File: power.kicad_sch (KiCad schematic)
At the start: 34 parts, among them J1 +5V SUPPLY, SW1 RESET, U1 NS32201, U2 LM3671, U3 NS32016, U4 NS32082, U5 NS32202, U6 74AHC08, Y1 12.00000MHz

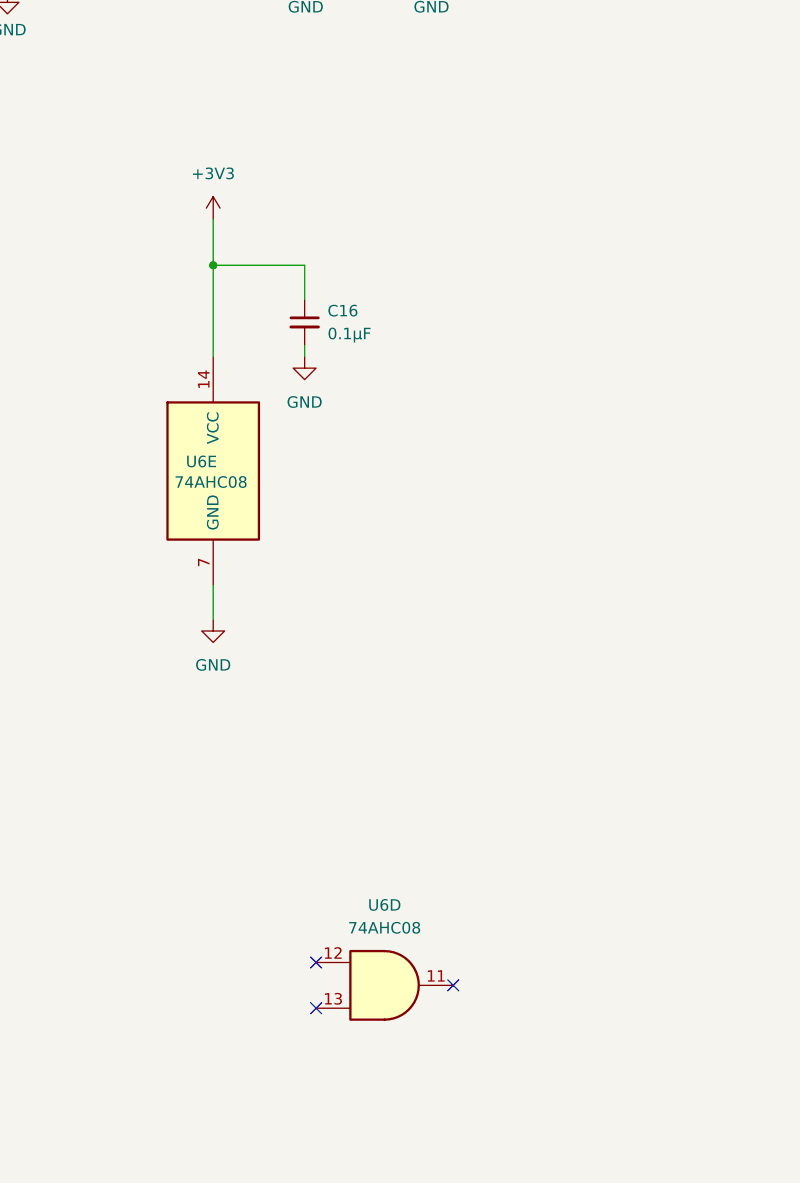
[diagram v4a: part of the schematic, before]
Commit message: add buffer to ICU
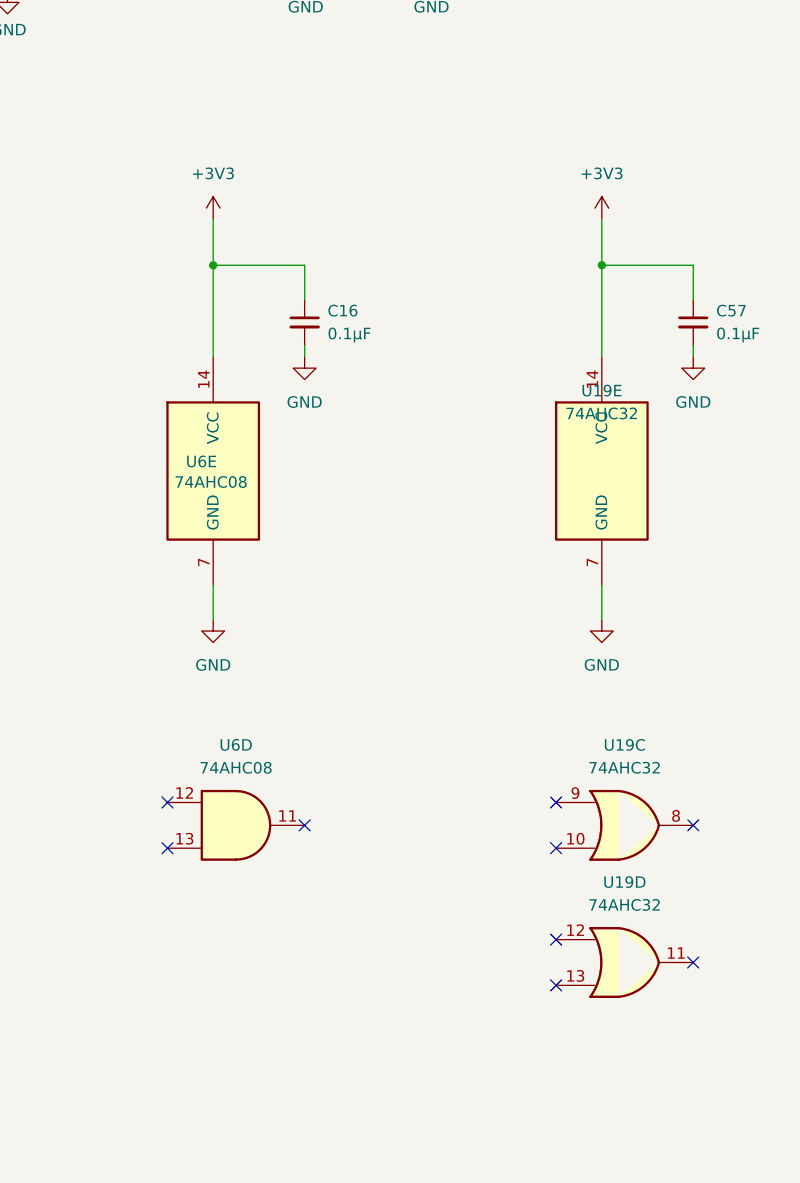
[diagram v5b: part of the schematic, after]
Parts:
- added C57: 0.1µF, Capacitor_SMD:C_0402_1005Metric, symbol Device:C_Small
- added U19: 74AHC32, Package_SO:TSSOP-14_4.4x5mm_P0.65mm, symbol 74xx:74LS32
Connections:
- net +3V3: now also C57.1, U19.14 (VCC)
- net GND: now also C57.2, U19.7 (GND)
- no-connect marks 4 -> 10
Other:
- moved on the sheet: U6D

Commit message: add 33uF 1206 16V reservoir cap to 5V
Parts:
- added C59: 33µF 16V, Capacitor_SMD:C_1206_3216Metric, symbol Device:C_Small
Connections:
- net +5V: now also C59.1
- net GND: now also C59.2
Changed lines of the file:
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@@
 	(wire
 		(pts
+			(xy 270.51 49.53) (xy 270.51 52.07)
+		)
+		(stroke
+			(width 0)
+			(type default)
+		)
+	)
+	(wire
+		(pts
 			(xy 147.32 43.18) (xy 147.32 40.64)
 		)
@@
 	(wire
 		(pts
+			(xy 270.51 41.91) (xy 270.51 44.45)
+		)
+		(stroke
+			(width 0)
+			(type default)
+		)
+	)
+	(wire
+		(pts
 			(xy 133.35 87.63) (xy 133.35 91.44)
 		)
@@
 	(symbol
 		(lib_id "power:GND")
+		(at 270.51 52.07 0)
+		(unit 1)
+		(exclude_from_sim no)
+		(in_bom yes)
+		(on_board yes)
+		(dnp no)
+		(fields_autoplaced yes)
+		(property "Reference" "#PWR0150"
+			(at 270.51 58.42 0)
+			(effects
+				(font
+					(size 1.27 1.27)
+				)
+				(hide yes)
+			)
+		)
+		(property "Value" "GND"
+			(at 270.51 57.15 0)
+			(effects
+				(font
+					(size 1.27 1.27)
+				)
+			)
+		)
+		(property "Footprint" ""
+			(at 270.51 52.07 0)
+			(effects
+				(font
+					(size 1.27 1.27)
+				)
+				(hide yes)
+			)
+		)
+		(property "Datasheet" ""
+			(at 270.51 52.07 0)
+			(effects
+				(font
+					(size 1.27 1.27)
+				)
+				(hide yes)
+			)
+		)
+		(property "Description" "Power symbol creates a global label with name \"GND\" , ground"
+			(at 270.51 52.07 0)
+			(effects
+				(font
+					(size 1.27 1.27)
+				)
+				(hide yes)
+			)
+		)
+		(pin "1"
+		)
+		(instances
+			(project ""
+				(path "/54787df0-1b8c-465f-acae-f55ec7f02da3/c6a0d4a9-2340-4a27-802f-10b03153dcd5"
+					(reference "#PWR0150")
+					(unit 1)
+				)
+			)
+		)
+	)
+	(symbol
+		(lib_id "power:GND")
 		(at 76.2 105.41 0)
 		(unit 1)
@@
 	)
 	(symbol
+		(lib_id "Device:C_Small")
+		(at 270.51 46.99 0)
+		(unit 1)
+		(exclude_from_sim no)
+		(in_bom yes)
+		(on_board yes)
+		(dnp no)
+		(fields_autoplaced yes)
+		(property "Reference" "C59"
+			(at 273.05 45.7262 0)
+			(effects
+				(font
+					(size 1.27 1.27)
+				)
+				(justify left)
+			)
+		)
+		(property "Value" "33µF 16V"
+			(at 273.05 48.2662 0)
+			(effects
+				(font
+					(size 1.27 1.27)
+				)
+				(justify left)
+			)
+		)
+		(property "Footprint" "Capacitor_SMD:C_1206_3216Metric"
+			(at 270.51 46.99 0)
+			(effects
+				(font
+					(size 1.27 1.27)
+				)
+				(hide yes)
+			)
+		)
+		(property "Datasheet" "~"
+			(at 270.51 46.99 0)
+			(effects
+				(font
+					(size 1.27 1.27)
+				)
+				(hide yes)
+			)
+		)
+		(property "Description" "Unpolarized capacitor, small symbol"
+			(at 270.51 46.99 0)
+			(effects
+				(font
+					(size 1.27 1.27)
+				)
+				(hide yes)
+			)
+		)
+		(pin "1"
+		)
+		(pin "2"
+		)
+		(instances
+			(project ""
+				(path "/54787df0-1b8c-465f-acae-f55ec7f02da3/c6a0d4a9-2340-4a27-802f-10b03153dcd5"
+					(reference "C59")
+					(unit 1)
+				)
+			)
+		)
+	)
+	(symbol
 		(lib_id "power:GND")
 		(at 147.32 58.42 0)
@@
 					(unit 1)
 				)
+			)
+		)
+	)
+	(symbol
+		(lib_id "power:+5V")
+		(at 270.51 41.91 0)
+		(unit 1)
+		(exclude_from_sim no)
+		(in_bom yes)
+		(on_board yes)
+		(dnp no)
+		(fields_autoplaced yes)
+		(property "Reference" "#PWR0151"
+			(at 270.51 45.72 0)
+			(effects
+				(font
+					(size 1.27 1.27)
+				)
+				(hide yes)
+			)
+		)
+		(property "Value" "+5V"
+			(at 270.51 36.83 0)
+			(effects
+				(font
+					(size 1.27 1.27)
+				)
+			)
+		)
+		(property "Footprint" ""
+			(at 270.51 41.91 0)
+			(effects
+				(font
+					(size 1.27 1.27)
+				)
+				(hide yes)
+			)
+		)
+		(property "Datasheet" ""
+			(at 270.51 41.91 0)
+			(effects
+				(font
+					(size 1.27 1.27)
+				)
+				(hide yes)
+			)
+		)
+		(property "Description" "Power symbol creates a global label with name \"+5V\""
+			(at 270.51 41.91 0)
+			(effects
+				(font
+					(size 1.27 1.27)
+				)
+				(hide yes)
+			)
+		)
+		(pin "1"
+		)
+		(instances
+			(project ""
+				(path "/54787df0-1b8c-465f-acae-f55ec7f02da3/c6a0d4a9-2340-4a27-802f-10b03153dcd5"
+					(reference "#PWR0151")
+					(unit 1)
+				)

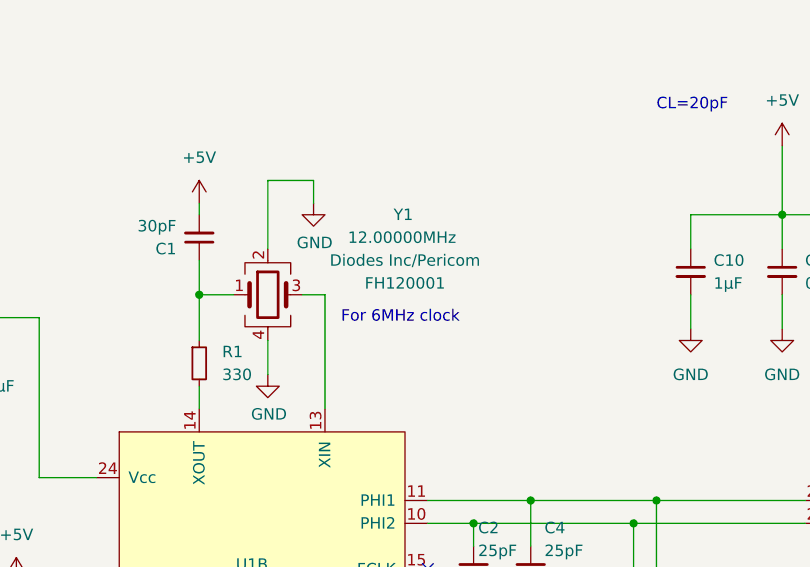
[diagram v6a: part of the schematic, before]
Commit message: fix ICU addressing error
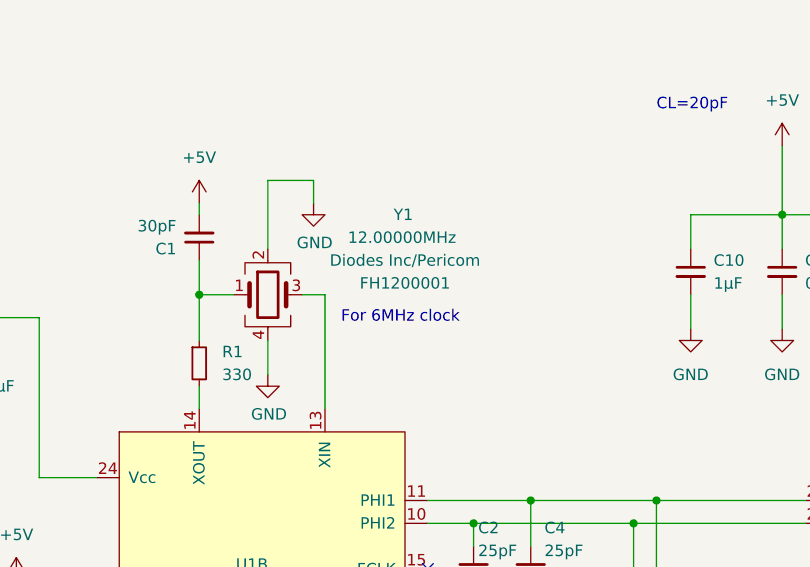
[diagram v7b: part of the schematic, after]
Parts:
- Y1: Part FH120001 -> FH1200001
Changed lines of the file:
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@@
 			)
 		)
-		(property "Part" "FH120001"
+		(property "Part" "FH1200001"
 			(at 91.44 95.25 0)
 			(effects
